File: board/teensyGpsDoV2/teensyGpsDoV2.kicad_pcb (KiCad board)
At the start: 2 copper layers, 2 parts, among them U1 Teensy4.0, X1 OSC5A2B02

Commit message: improvements
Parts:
- added C1: 10u, Capacitor_THT:CP_Radial_Tantal_D5.0mm_P5.00mm, F.Cu at (55.6, 106.5)
- added C2: 10u, Capacitor_THT:CP_Radial_Tantal_D5.0mm_P5.00mm, F.Cu at (55.6, 115.0)
- added J1: Barrel_Jack, Connector_BarrelJack:BarrelJack_SwitchcraftConxall_RAPC10U_Horizontal, F.Cu at (83.3, 92.7)
- added J2: NPPN042AFCN-RC, NPPN042AFCN-RC:CONN4x2_NPPN042AFCN-RC_SUL, F.Cu at (114.5, 100.0)
- added R1: 330, Resistor_THT:R_Axial_DIN0207_L6.3mm_D2.5mm_P7.62mm_Horizontal, F.Cu at (64.0, 104.3)
- added R3: 100, Resistor_THT:R_Axial_DIN0207_L6.3mm_D2.5mm_P7.62mm_Horizontal, F.Cu at (64.0, 108.4)
- added R4: 100, Resistor_THT:R_Axial_DIN0207_L6.3mm_D2.5mm_P7.62mm_Horizontal, F.Cu at (64.0, 112.4)
- added R5: 100, Resistor_THT:R_Axial_DIN0207_L6.3mm_D2.5mm_P7.62mm_Horizontal, F.Cu at (64.0, 116.5)
- added U2: LT1086-5.0, Package_TO_SOT_THT:TO-220-3_Vertical, F.Cu at (97.5, 56.0)
- added U3: DAC8550IxDGK, Package_SON:VSON-8-1EP_3x3mm_P0.65mm_EP1.65x2.4mm, F.Cu at (86.5, 110.5)
- moved X1 22.2 mm to (78.5, 43.0)
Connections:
- U1 pad 12: unconnected-(U1-10_CS_MQSR-Pad12) -> Net-(U1-10_CS_MQSR)
- U1 pad 13: unconnected-(U1-11_MOSI_CTX1-Pad13) -> Net-(U1-11_MOSI_CTX1)
- U1 pad 20: unconnected-(U1-13_SCK_CRX1_LED-Pad20) -> Net-(U1-13_SCK_CRX1_LED)
- U1 pad 25: unconnected-(U1-18_A4_SDA0-Pad25) -> pps
- U1 pad 26: unconnected-(U1-19_A5_SCL0-Pad26) -> 10 MHz
- U1 pad 27: unconnected-(U1-20_A6_TX5_LRCLK1-Pad27) -> Net-(U1-20_A6_TX5_LRCLK1)
- U1 pad 28: unconnected-(U1-21_A7_RX5_BCLK1-Pad28) -> Net-(U1-21_A7_RX5_BCLK1)
- U1 pad 31: unconnected-(U1-3V3-Pad31) -> +3.3V
- U1 pad 33: unconnected-(U1-VIN-Pad33) -> /5V Teensy
- X1 pad 1: unconnected-(X1-OUT-Pad1) -> 10 MHz
- X1 pad 2: unconnected-(X1-GND-Pad2) -> GND
- X1 pad 3: unconnected-(X1-VCTRL-Pad3) -> Net-(U3-V_{FB})
- X1 pad 5: unconnected-(X1-VCC-Pad5) -> +5V

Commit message: layout wip
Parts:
- added C1: 1uF, Capacitor_THT:C_Disc_D5.0mm_W2.5mm_P5.00mm, F.Cu at (140.0, 69.0)
- added C10: 10uF, Capacitor_THT:C_Disc_D5.0mm_W2.5mm_P5.00mm, F.Cu at (161.1, 50.5)
- added C11: .1uF, Capacitor_THT:C_Disc_D5.0mm_W2.5mm_P5.00mm, F.Cu at (161.1, 55.5)
- added C12: 1uF, Capacitor_THT:C_Disc_D5.0mm_W2.5mm_P5.00mm, F.Cu at (136.6, 59.0)
- added C13: 1uF, Capacitor_THT:C_Disc_D5.0mm_W2.5mm_P5.00mm, F.Cu at (128.6, 59.0)
- added C2: 1uF, Capacitor_THT:C_Disc_D5.0mm_W2.5mm_P5.00mm, F.Cu at (140.0, 74.0)
- added C5: 10uF, Capacitor_THT:C_Disc_D5.0mm_W2.5mm_P5.00mm, F.Cu at (148.5, 69.0)
- added C6: .1uF, Capacitor_THT:C_Disc_D5.0mm_W2.5mm_P5.00mm, F.Cu at (148.5, 74.0)
- added C7: 10uF, Capacitor_THT:C_Disc_D5.0mm_W2.5mm_P5.00mm, F.Cu at (140.0, 79.0)
- added C8: 10uF, Capacitor_THT:C_Disc_D5.0mm_W2.5mm_P5.00mm, F.Cu at (148.5, 79.0)
- added C9: .1uF, Capacitor_THT:C_Disc_D5.0mm_W2.5mm_P5.00mm, F.Cu at (144.6, 101.0)
- added D1: PPS LED, LED_THT:LED_D5.0mm_Clear, F.Cu at (112.1, 51.5)
- added D2: Lock LED, LED_THT:LED_D5.0mm_Clear, F.Cu at (129.8, 51.5)
- added FB1: 133 @ 100 MHz, Resistor_THT:R_Axial_DIN0411_L9.9mm_D3.6mm_P12.70mm_Horizontal, F.Cu at (172.1, 55.0)
- added FB2: 133 @ 100 MHz, Resistor_THT:R_Axial_DIN0411_L9.9mm_D3.6mm_P12.70mm_Horizontal, F.Cu at (172.1, 50.5)
- added FB3: 133 @ 100 MHz, Resistor_THT:R_Axial_DIN0411_L9.9mm_D3.6mm_P12.70mm_Horizontal, F.Cu at (127.2, 101.0)
- added H1: MountingHole, MountingHole:MountingHole_3.5mm_Pad, F.Cu at (103.6, 50.5)
- added H2: MountingHole, MountingHole:MountingHole_3.5mm_Pad, F.Cu at (194.6, 50.5)
- added H3: MountingHole, MountingHole:MountingHole_3.5mm_Pad, F.Cu at (103.6, 141.5)
- added H4: MountingHole, MountingHole:MountingHole_3.5mm_Pad, F.Cu at (194.6, 141.5)
- added J3: LCD_Header, Connector_PinHeader_2.54mm:PinHeader_1x04_P2.54mm_Vertical, F.Cu at (167.8, 141.5)
- added J4: 10MHz Out, Connector_Coaxial:SMA_Wurth_60312002114503_Vertical, F.Cu at (183.8, 96.7)
- added J5: 1PPS Out, Connector_Coaxial:SMA_Wurth_60312002114503_Vertical, F.Cu at (192.5, 88.5)
- added JP1: OSC_VCTRL_SEL, Connector_PinHeader_2.54mm:PinHeader_1x03_P2.54mm_Vertical, F.Cu at (153.1, 50.0)
- added JP2: DAC_VREF_SEL, Connector_PinHeader_2.54mm:PinHeader_1x03_P2.54mm_Vertical, F.Cu at (157.1, 50.0)
- added R10: 33, Resistor_THT:R_Axial_DIN0207_L6.3mm_D2.5mm_P10.16mm_Horizontal, F.Cu at (128.5, 89.5)
- added R11: 33, Resistor_THT:R_Axial_DIN0207_L6.3mm_D2.5mm_P10.16mm_Horizontal, F.Cu at (141.5, 89.5)
- added R12: 33, Resistor_THT:R_Axial_DIN0207_L6.3mm_D2.5mm_P10.16mm_Horizontal, F.Cu at (128.5, 95.0)
- added R13: 100, Resistor_THT:R_Axial_DIN0207_L6.3mm_D2.5mm_P10.16mm_Horizontal, F.Cu at (141.4, 95.0)
- added R14: 100, Resistor_THT:R_Axial_DIN0207_L6.3mm_D2.5mm_P10.16mm_Horizontal, F.Cu at (167.5, 97.5)
- added R15: 100, Resistor_THT:R_Axial_DIN0207_L6.3mm_D2.5mm_P10.16mm_Horizontal, F.Cu at (167.5, 92.5)
- added R16: 4.7k, Resistor_THT:R_Axial_DIN0207_L6.3mm_D2.5mm_P10.16mm_Horizontal, F.Cu at (167.5, 87.5)
- added R17: 220, Resistor_THT:R_Axial_DIN0207_L6.3mm_D2.5mm_P10.16mm_Horizontal, F.Cu at (120.1, 59.6)
- added R18: 220, Resistor_THT:R_Axial_DIN0207_L6.3mm_D2.5mm_P10.16mm_Horizontal, F.Cu at (125.1, 59.6)
- added R19: 4.7k, Resistor_THT:R_Axial_DIN0207_L6.3mm_D2.5mm_P10.16mm_Horizontal, F.Cu at (179.5, 139.0)
- added R2: 100, Resistor_THT:R_Axial_DIN0207_L6.3mm_D2.5mm_P10.16mm_Horizontal, F.Cu at (162.6, 69.5)
- added R20: 4.7k, Resistor_THT:R_Axial_DIN0207_L6.3mm_D2.5mm_P10.16mm_Horizontal, F.Cu at (179.7, 143.8)
- added R6: 33, Resistor_THT:R_Axial_DIN0207_L6.3mm_D2.5mm_P10.16mm_Horizontal, F.Cu at (194.8, 70.4)
- added R7: 100, Resistor_THT:R_Axial_DIN0207_L6.3mm_D2.5mm_P10.16mm_Horizontal, F.Cu at (142.5, 64.0)
- added R8: 20k, Resistor_THT:R_Axial_DIN0207_L6.3mm_D2.5mm_P10.16mm_Horizontal, F.Cu at (128.5, 84.0)
- added R9: 20k, Resistor_THT:R_Axial_DIN0207_L6.3mm_D2.5mm_P10.16mm_Horizontal, F.Cu at (141.6, 84.0)
- added SW1: SW_SPDT, Connector_PinSocket_2.54mm:PinSocket_1x03_P2.54mm_Vertical, F.Cu at (104.6, 59.5)
- added U1: LM2596_Module, LM2596_Module:YAAJ_DCDC_StepDown_LM2596, F.Cu at (104.2, 125.8)
- added U2: MCP1703, Package_TO_SOT_THT:TO-92_Inline, F.Cu at (138.6, 52.0)
- added U5: 74HC14, Package_DIP:DIP-14_W7.62mm_Socket, F.Cu at (156.1, 86.0)
- added U7: REF3333, Package_TO_SOT_SMD:SOT-23, F.Cu at (147.5, 52.0)
- J1: value Barrel_Jack -> Screw_Terminal_01x02; footprint Connector_BarrelJack:BarrelJack_SwitchcraftConxall_RAPC10U_Horizontal -> TerminalBlock:TerminalBlock_MaiXu_MX126-5.0-02P_1x02_P5.00mm
- J2: value NPPN042AFCN-RC -> GPS Connector
- R1: value 330 -> 100; footprint Resistor_THT:R_Axial_DIN0207_L6.3mm_D2.5mm_P7.62mm_Horizontal -> Resistor_THT:R_Axial_DIN0207_L6.3mm_D2.5mm_P10.16mm_Horizontal
- R3: footprint Resistor_THT:R_Axial_DIN0207_L6.3mm_D2.5mm_P7.62mm_Horizontal -> Resistor_THT:R_Axial_DIN0207_L6.3mm_D2.5mm_P10.16mm_Horizontal
- R4: value 100 -> 330; footprint Resistor_THT:R_Axial_DIN0207_L6.3mm_D2.5mm_P7.62mm_Horizontal -> Resistor_THT:R_Axial_DIN0207_L6.3mm_D2.5mm_P10.16mm_Horizontal
- R5: value 100 -> 680; footprint Resistor_THT:R_Axial_DIN0207_L6.3mm_D2.5mm_P7.62mm_Horizontal -> Resistor_THT:R_Axial_DIN0207_L6.3mm_D2.5mm_P10.16mm_Horizontal
- U4: renamed from U3; value DAC8550IxDGK -> DAC8550
- moved R5 143.5 mm to (194.8, 57.4), turned to -90 degrees
- moved R4 103.0 mm to (162.6, 82.6), turned to 90 degrees
- moved X1 102.9 mm to (177.6, 71.0)
- moved C4 102.9 mm to (155.1, 141.5)
- moved R1 99.8 mm to (157.6, 69.6), turned to 90 degrees
- moved R3 97.1 mm to (157.6, 82.6), turned to 90 degrees
- moved C3 96.5 mm to (145.6, 141.5)
- moved U3 92.9 mm to (138.1, 139.5), turned to 180 degrees
- moved U4 80.3 mm to (147.3, 58.1)
- moved J1 57.3 mm to (114.8, 140.7)
- moved J2 28.9 mm to (133.2, 122.0), turned to 90 degrees
- moved U6 3.42 mm to (120.6, 71.5)
- renumbered C1 to C3, C2 to C4, U2 to U3, U1 to U6
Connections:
- net Net-(U1-20_A6_TX5_LRCLK1) renamed MCU_TO_GPS_UART
- net Net-(U1-21_A7_RX5_BCLK1) renamed GPS_TO_MCU_UART
- C3 pad 1: Net-(U2-VI) -> Net-(J1-Pin_2)
- C4 pad 1: +5V -> +5VD
- J1 pad 1: Net-(U2-VI) -> GND
- J1 pad 2: GND -> Net-(J1-Pin_2)
- J2 pad 6: pps -> Net-(J2-Pad6)
- R1 pad 1: 10 MHz -> DAC_DAT_CLK
- R1 pad 2: Net-(R1-Pad2) -> Net-(U4-SCLK)
- R3 pad 1: Net-(U1-13_SCK_CRX1_LED) -> DAC_CS
- R3 pad 2: Net-(U3-SCLK) -> Net-(U4-~{SYNC})
- R4 pad 1: Net-(U1-11_MOSI_CTX1) -> Net-(X1-OUT)
- R4 pad 2: Net-(U3-D_{IN}) -> Net-(R4-Pad2)
- R5 pad 1: Net-(U1-10_CS_MQSR) -> Net-(R4-Pad2)
- R5 pad 2: Net-(U3-~{SYNC}) -> GND
- U3 pad 2: +5V -> +5VD
- U3 pad 3: Net-(U2-VI) -> Net-(J1-Pin_2)
- U4 pad 1: +3.3V -> Net-(U4-V_{DD})
- U4 pad 2: unconnected-(U3-V_{REF}-Pad2) -> Net-(JP2-C)
- U4 pad 3: Net-(U3-V_{FB}) -> DAC OSC VCTRL
- U4 pad 4: Net-(U3-V_{FB}) -> DAC OSC VCTRL
- U4 pad 5: Net-(U3-~{SYNC}) -> Net-(U4-~{SYNC})
- U4 pad 6: Net-(U3-SCLK) -> Net-(U4-SCLK)
- U4 pad 7: Net-(U3-D_{IN}) -> Net-(U4-D_{IN})
- U6 pad 12: Net-(U1-10_CS_MQSR) -> DAC_CS
- U6 pad 13: Net-(U1-11_MOSI_CTX1) -> DAC_DAT
- U6 pad 20: Net-(U1-13_SCK_CRX1_LED) -> DAC_DAT_CLK
- U6 pad 21: unconnected-(U1-14_A0_TX3_SPDIF_OUT-Pad21) -> PPS_LED
- U6 pad 22: unconnected-(U1-15_A1_RX3_SPDIF_IN-Pad22) -> LOCK_LED
- U6 pad 23: unconnected-(U1-16_A2_RX4_SCL1-Pad23) -> LCD_SCL
- U6 pad 24: unconnected-(U1-17_A3_TX4_SDA1-Pad24) -> LCD_SDA
- U6 pad 25: pps -> 1PPS
- U6 pad 26: 10 MHz -> 10MHz_MCU
- U6 pad 33: /5V Teensy -> Net-(SW1-B)
- U6 pad 5: unconnected-(U1-3_LRCLK2-Pad5) -> PWM_OSC_TUNE
- X1 pad 1: 10 MHz -> Net-(X1-OUT)
- X1 pad 3: Net-(U3-V_{FB}) -> Net-(X1-VCTRL)
- X1 pad 5: +5V -> Net-(X1-VCC)
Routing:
- added copper zone on B.Cu, net GND
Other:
- board outline added: 100 x 100 mm

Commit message: wip schematic, routing
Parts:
- SW1: footprint Connector_PinSocket_2.54mm:PinSocket_1x03_P2.54mm_Vertical -> Connector_PinHeader_2.54mm:PinHeader_1x03_P2.54mm_Vertical
- moved D1 17.9 mm to (130.0, 51.5)
- moved D2 17.8 mm to (112.0, 51.5)
- moved R5 10.1 mm to (194.8, 67.5), turned to 90 degrees
- moved R8 10.0 mm to (138.5, 84.0), turned to 180 degrees
- moved R18 5.08 mm to (120.0, 59.6)
- moved R17 4.92 mm to (125.0, 59.6)
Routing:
- net +5VA: track 0.00 -> 213.0 mm
- net +3.3V: track 0.00 -> 209.5 mm, vias 0 -> 2
- net +5VD: track 0.00 -> 141.0 mm
- net LCD_SDA: track 0.00 -> 115.9 mm
- net LCD_SCL: track 0.00 -> 112.8 mm
- net Net-(J2-Pad6): track 0.00 -> 74.8 mm, vias 0 -> 1
- net 1PPS: track 0.00 -> 73.8 mm, vias 0 -> 3
- net Net-(U4-V_{DD}): track 0.00 -> 69.3 mm, vias 0 -> 1
- net MCU_TO_GPS_UART: track 0.00 -> 68.8 mm, vias 0 -> 1
- net GPS_TO_MCU_UART: track 0.00 -> 68.1 mm
- net Net-(J1-Pin_2): track 0.00 -> 48.8 mm
- net 10MHz_MCU: track 0.00 -> 48.7 mm
- net 10MHz_Raw: track 0.00 -> 48.5 mm
- net Net-(JP1-C): track 0.00 -> 45.6 mm
- net Net-(R12-Pad1): track 0.00 -> 42.8 mm, vias 0 -> 2
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
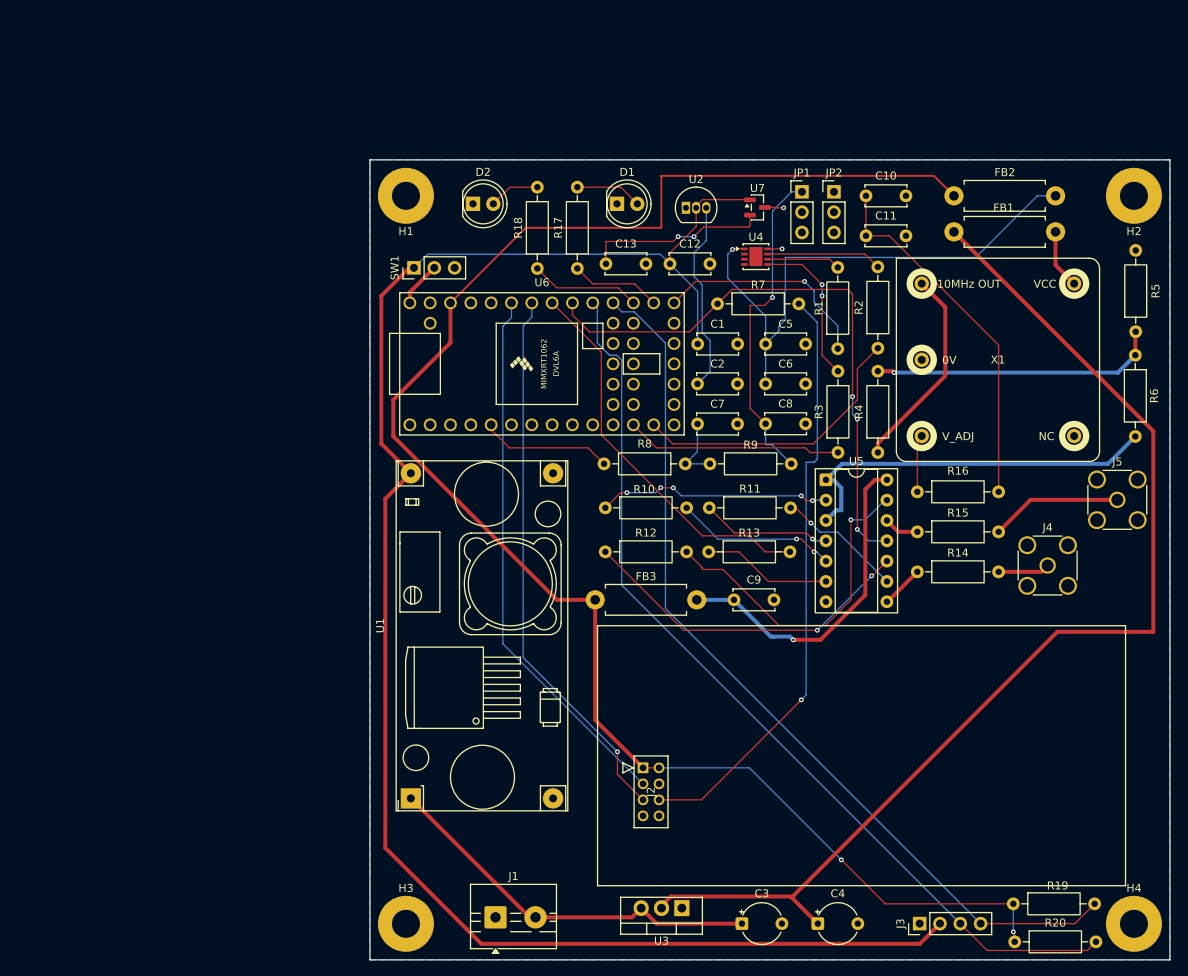
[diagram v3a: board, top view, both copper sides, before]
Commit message: schematic routing done, allegedly
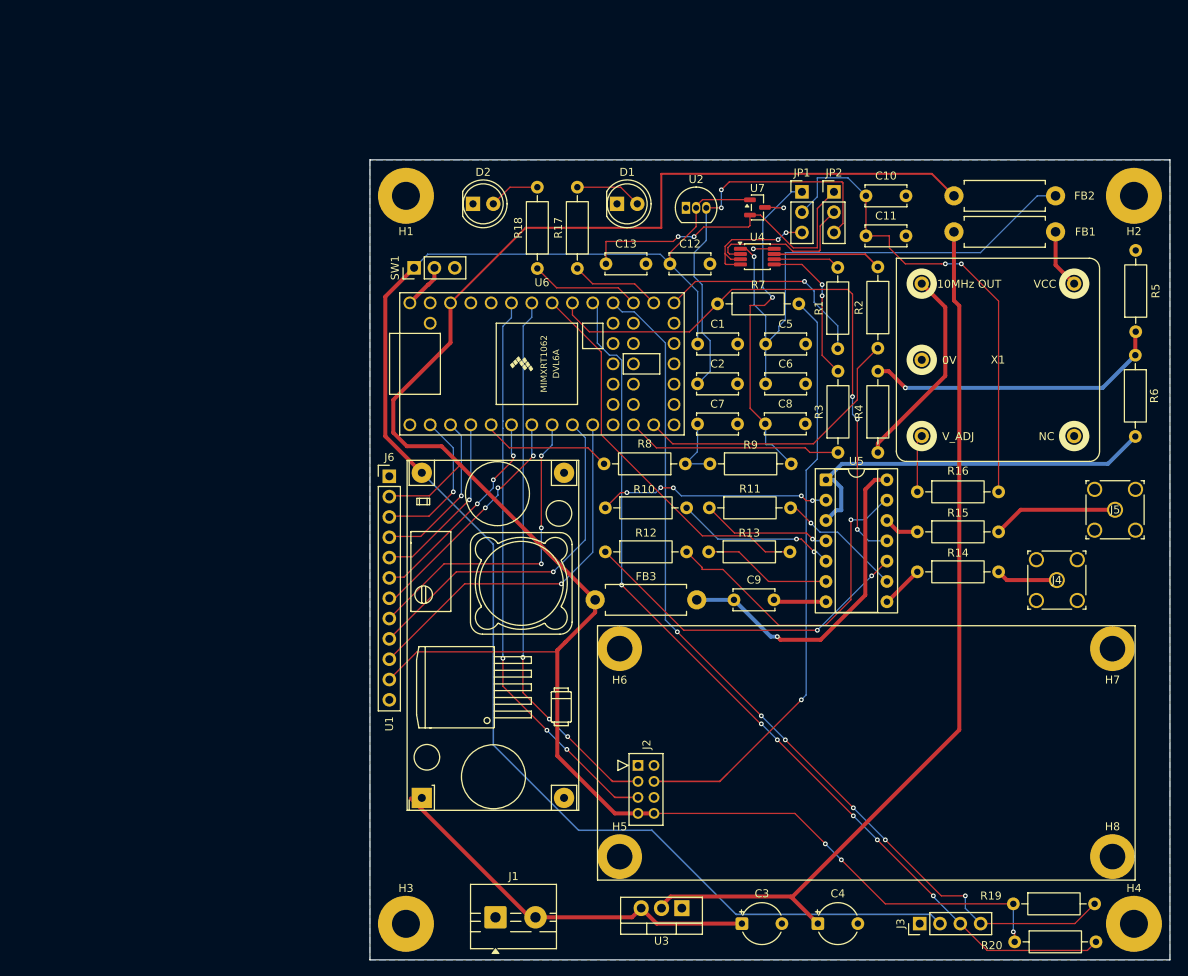
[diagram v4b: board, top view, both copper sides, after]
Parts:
- added H5: GPS_MountingHole, MountingHole:MountingHole_3.2mm_M3_DIN965_Pad, F.Cu at (130.3, 133.1)
- added H6: GPS_MountingHole, MountingHole:MountingHole_3.2mm_M3_DIN965_Pad, F.Cu at (130.3, 107.1)
- added H7: GPS_MountingHole, MountingHole:MountingHole_3.2mm_M3_DIN965_Pad, F.Cu at (191.9, 107.1)
- added H8: GPS_MountingHole, MountingHole:MountingHole_3.2mm_M3_DIN965_Pad, F.Cu at (191.9, 133.1)
- added J6: Conn_01x12_Pin, Connector_PinHeader_2.54mm:PinHeader_1x12_P2.54mm_Vertical, F.Cu at (101.5, 85.6)
- J4, J5: footprint Connector_Coaxial:SMA_Wurth_60312002114503_Vertical -> RF2-04A-T-00-50-G:CONN_RF2-04A-T-00-50-G_ADM
- U4: footprint Package_SON:VSON-8-1EP_3x3mm_P0.65mm_EP1.65x2.4mm -> Package_SO:VSSOP-8_3x3mm_P0.65mm
- moved J4 2.15 mm to (184.9, 98.5)
- moved U1 1.37 mm to (105.6, 125.8)
- moved J5 1.27 mm to (192.2, 89.7)
- moved J2 0.70 mm to (132.6, 121.7)
- moved U4 0.17 mm to (147.5, 58.1)
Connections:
- J2 pad 1: +3.3V -> unconnected-(J2-Pad1)
- J2 pad 2: +3.3V -> GND
- J2 pad 3: GPS_TO_MCU_UART -> MCU_TO_GPS_UART
- J2 pad 4: unconnected-(J2-Pad4) -> Net-(J2-Pad4)
- J2 pad 5: MCU_TO_GPS_UART -> GPS_TO_MCU_UART
- J2 pad 6: Net-(J2-Pad6) -> unconnected-(J2-Pad6)
- J2 pad 7: unconnected-(J2-Pad7) -> +3.3V
- J2 pad 8: GND -> +3.3V
- J4 pad 2: unconnected-(J4-Ext-Pad2) -> GND
- J5 pad 2: unconnected-(J5-Ext-Pad2) -> GND
- R7 pad 2: Net-(J2-Pad6) -> Net-(J2-Pad4)
- U4 pad 3: DAC OSC VCTRL -> DAC_OSC_VCTRL
- U4 pad 4: DAC OSC VCTRL -> DAC_OSC_VCTRL
- U6 pad 1: unconnected-(U6-GND-Pad1) -> GND
- U6 pad 10: unconnected-(U6-8_TX2_IN1-Pad10) -> Net-(J6-Pin_10)
- U6 pad 2: unconnected-(U6-0_RX1_CRX2_CS1-Pad2) -> Net-(J6-Pin_3)
- U6 pad 3: unconnected-(U6-1_TX1_CTX2_MISO1-Pad3) -> Net-(J6-Pin_4)
- U6 pad 32: unconnected-(U6-GND-Pad32) -> GND
- U6 pad 4: unconnected-(U6-2_OUT2-Pad4) -> Net-(J6-Pin_5)
- U6 pad 6: unconnected-(U6-4_BCLK2-Pad6) -> Net-(J6-Pin_6)
- U6 pad 7: unconnected-(U6-5_IN2-Pad7) -> Net-(J6-Pin_7)
- U6 pad 8: unconnected-(U6-6_OUT1D-Pad8) -> Net-(J6-Pin_8)
- U6 pad 9: unconnected-(U6-7_RX2_OUT1A-Pad9) -> Net-(J6-Pin_9)
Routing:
- net Net-(J2-Pad6): track 74.8 -> 0.00 mm, vias 1 -> 0
- net Net-(J2-Pad4): track 0.00 -> 73.9 mm, vias 0 -> 1
- net Net-(J6-Pin_10): track 0.00 -> 46.9 mm, vias 0 -> 1
- net Net-(J6-Pin_9): track 0.00 -> 45.4 mm, vias 0 -> 1
- net +3.3V: track 209.5 -> 253.3 mm, vias 2 -> 3
- net Net-(J6-Pin_8): track 0.00 -> 39.8 mm, vias 0 -> 3
- net Net-(J6-Pin_7): track 0.00 -> 30.0 mm, vias 0 -> 3
- net +5VD: track 141.0 -> 113.9 mm
- net Net-(J6-Pin_6): track 0.00 -> 26.8 mm, vias 0 -> 3
- net DAC_VREF_LDO: track 24.1 -> 50.6 mm, vias 0 -> 2
- net Net-(J6-Pin_5): track 0.00 -> 22.6 mm, vias 0 -> 1
- net +5VA: track 213.0 -> 192.1 mm
- net Net-(J6-Pin_4): track 0.00 -> 20.7 mm, vias 0 -> 1
- net Net-(JP2-C): track 0.00 -> 19.9 mm
- net Net-(J6-Pin_3): track 0.00 -> 19.0 mm, vias 0 -> 1
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
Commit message: revision 1.0 submitted for manufacturing
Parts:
- moved H8 1.11 mm to (190.8, 133.1)
- moved H7 1.10 mm to (190.8, 107.1)
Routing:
- net Net-(R12-Pad1): track 42.8 -> 52.9 mm, vias 2 -> 3
- net GND: track 11.8 -> 5.53 mm
- net +5VA: track 192.1 -> 195.2 mm, vias 0 -> 3
- net DAC_OSC_VCTRL: track 16.6 -> 18.0 mm, vias 2 -> 1
- net DAC_VREF_LDO: track 50.6 -> 51.9 mm
- net +3.3V: track 253.3 -> 252.2 mm, vias 3 -> 5
- net Net-(U5G-VCC): track 41.9 -> 42.5 mm
- net DAC_VREF_REF: track 41.1 -> 41.7 mm
- net Net-(R12-Pad2): track 41.3 -> 40.8 mm
- net PWM_OSC_VCTRL: track 42.0 -> 41.5 mm
- net Net-(J2-Pad4): track 73.9 -> 74.1 mm, vias 1 -> 5
- net Net-(R10-Pad1): vias 5 -> 2
- net Net-(R11-Pad1): vias 1 -> 0
- net Net-(R10-Pad2): vias 2 -> 0
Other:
- board text added: "1 PPS"
- board text added: "10 MHz"
- board text added: "6-9v"
- board text added: "DAC"
- board text added: "GND"
- board text added: "LCD"
- board text added: "LDO"
- board text added: "LEA-5T Module"
- board text added: "LOCK LED"
- board text added: "OSC5A2B02"
- board text added: "PPS LED"
- board text added: "PWM"
- board text added: "REF"
- board text added: "RRR III 2025"
- board text added: "Teensy 4.0 GPSDO v1.0"
- board text added: "VA"
- board text added: "VUSB"
